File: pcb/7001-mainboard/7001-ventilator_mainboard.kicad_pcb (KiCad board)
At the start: 4 copper layers, 84 parts, among them J1 USB_B_Micro, J10 UART, J2 SWD, J3 Conn_01x02_MountingPin, J4 DNI, J6 5V out, J9 Raspberry_Pi_2_3, Q1 IRLML6244TRPbF, U1 MPRLS0001PG0000SA, U10 ABPMAND001PG2A3, U11 MPVZ5010GW6U, U12 MPVZ5010GW6U, U2 TPD2E2U06, U3 LPC11U37FBD48-401_, U4 MCP1825S, U7 AD5410AREZ, U8 MPRLS0001PG0000SA, U9 ABPMAND001PG2A3, Y1 MCSJK-7U-12.00-10-10-80-B-10

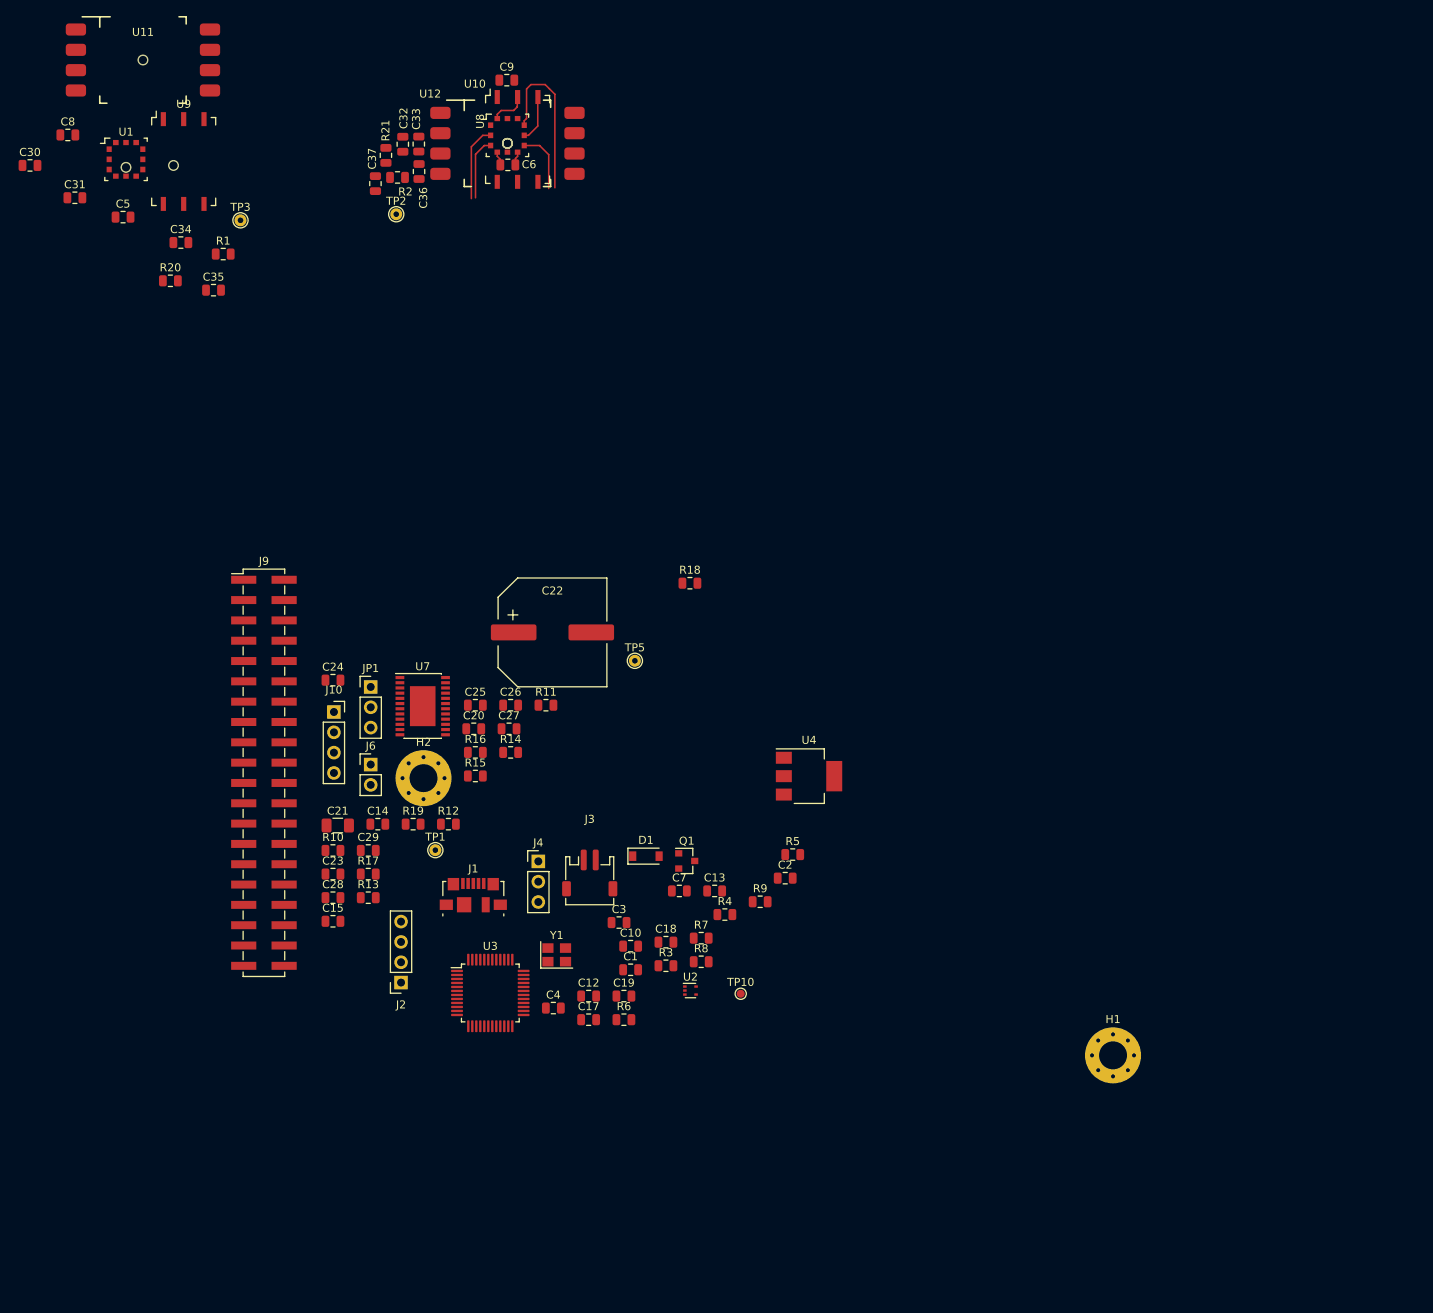
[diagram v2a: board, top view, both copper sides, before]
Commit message: Schematics/PCB: add screw terminal footprints
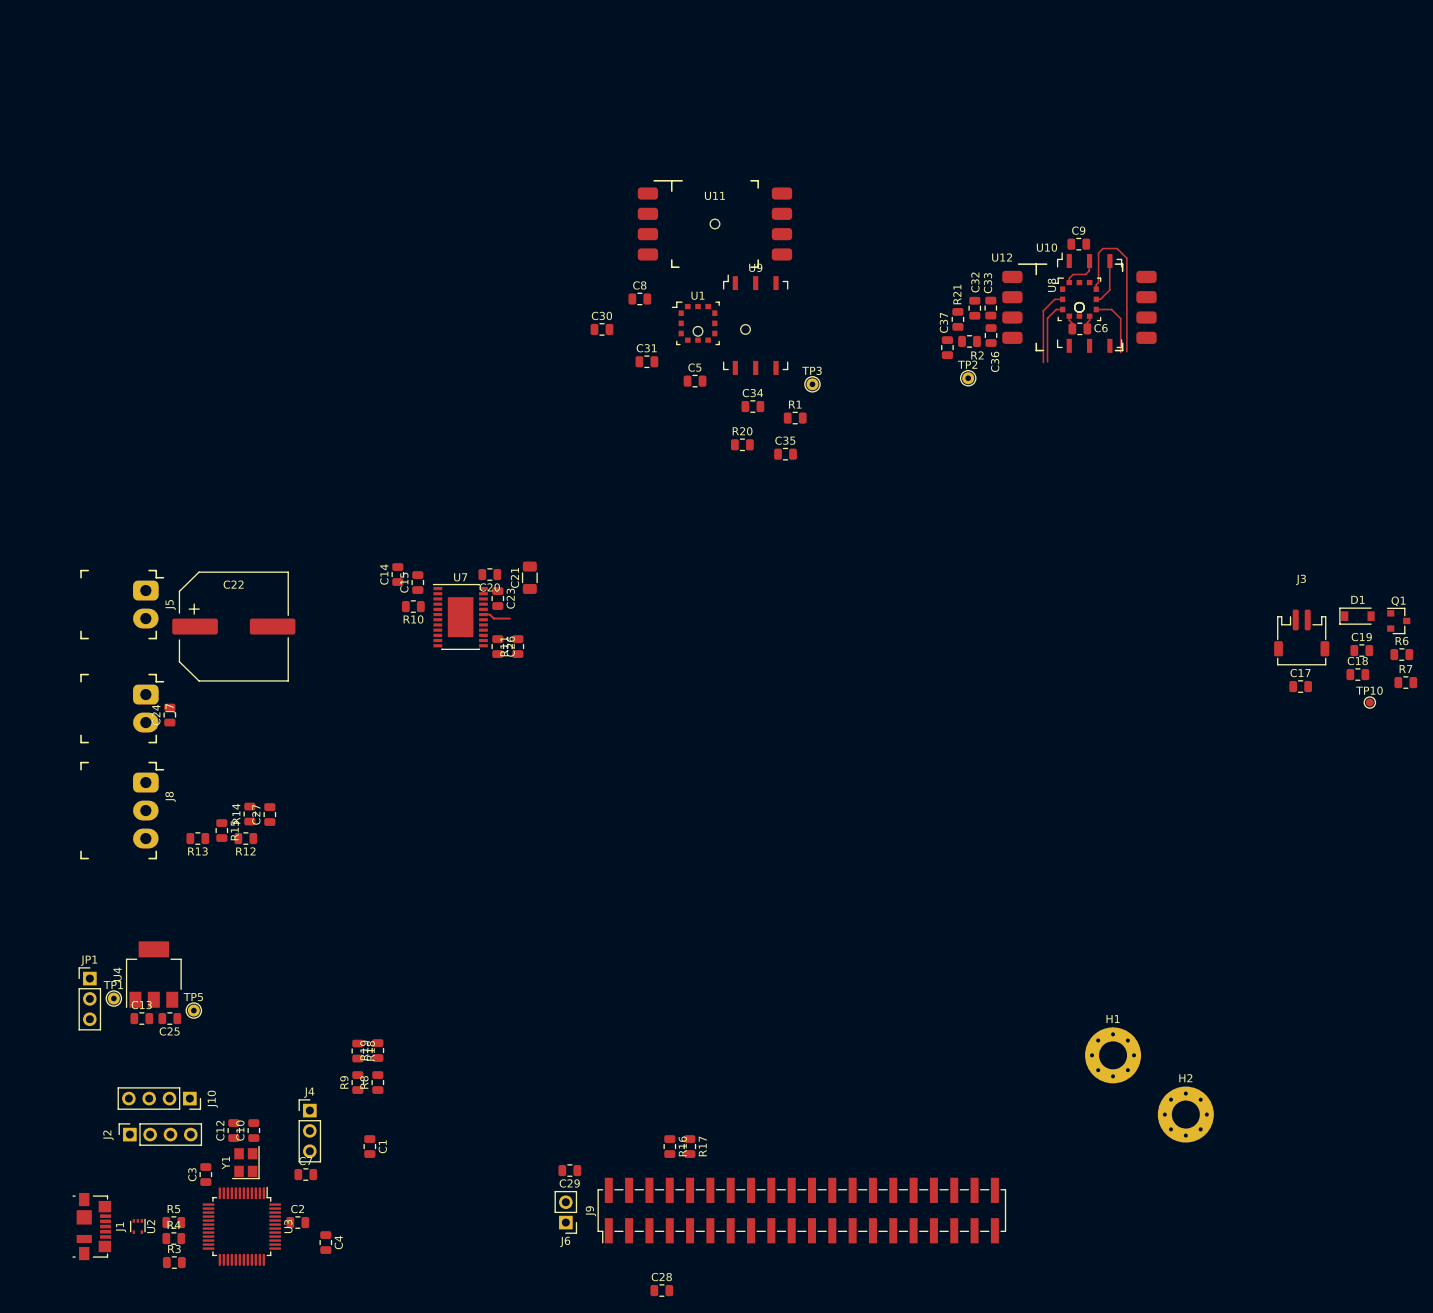
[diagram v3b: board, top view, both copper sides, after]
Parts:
- added J5: 24VIN, Jitter_Footprints:TerminalBlock_Wurth_WR-TBL_691322110002_1x02_P3.50mm_Horizontal, F.Cu at (30.0, 22.0)
- added J7: PREG_PWR, Jitter_Footprints:TerminalBlock_Wurth_WR-TBL_691322110002_1x02_P3.50mm_Horizontal, F.Cu at (30.0, 35.0)
- added J8: PREG_SIGNALS, Jitter_Footprints:TerminalBlock_Wurth_WR-TBL_691322110003_1x03_P3.50mm_Horizontal, F.Cu at (30.0, 46.0)
- moved R6 107.4 mm to (187.0, 30.0)
- moved H2 104.2 mm to (160.0, 87.5)
- moved C19 101.9 mm to (182.0, 29.5)
- moved C17 98.3 mm to (174.3, 34.0)
- moved J3 93.9 mm to (174.5, 28.3)
- moved Q1 93.9 mm to (186.6, 25.8)
- moved D1 93.9 mm to (181.5, 25.2)
- moved R7 93.7 mm to (187.5, 33.5)
- moved C18 92.7 mm to (181.5, 32.5)
- moved R5 90.0 mm to (33.5, 101.0)
- moved J9 86.7 mm to (112.0, 99.5), turned to 90 degrees
- moved TP10 86.7 mm to (183.0, 36.0)
- moved U4 85.6 mm to (31.0, 70.0), turned to 90 degrees
- moved R4 79.9 mm to (33.5, 103.0)
- moved U2 75.1 mm to (29.0, 101.5), turned to 270 degrees
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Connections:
- R13 pad 2: (no net) -> /I_PREG_FEEDBACK
- U7 pad 19: (no net) -> /I_PREG_SETPOINT
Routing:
- net /I_PREG_SETPOINT: track 0.00 -> 3.51 mm

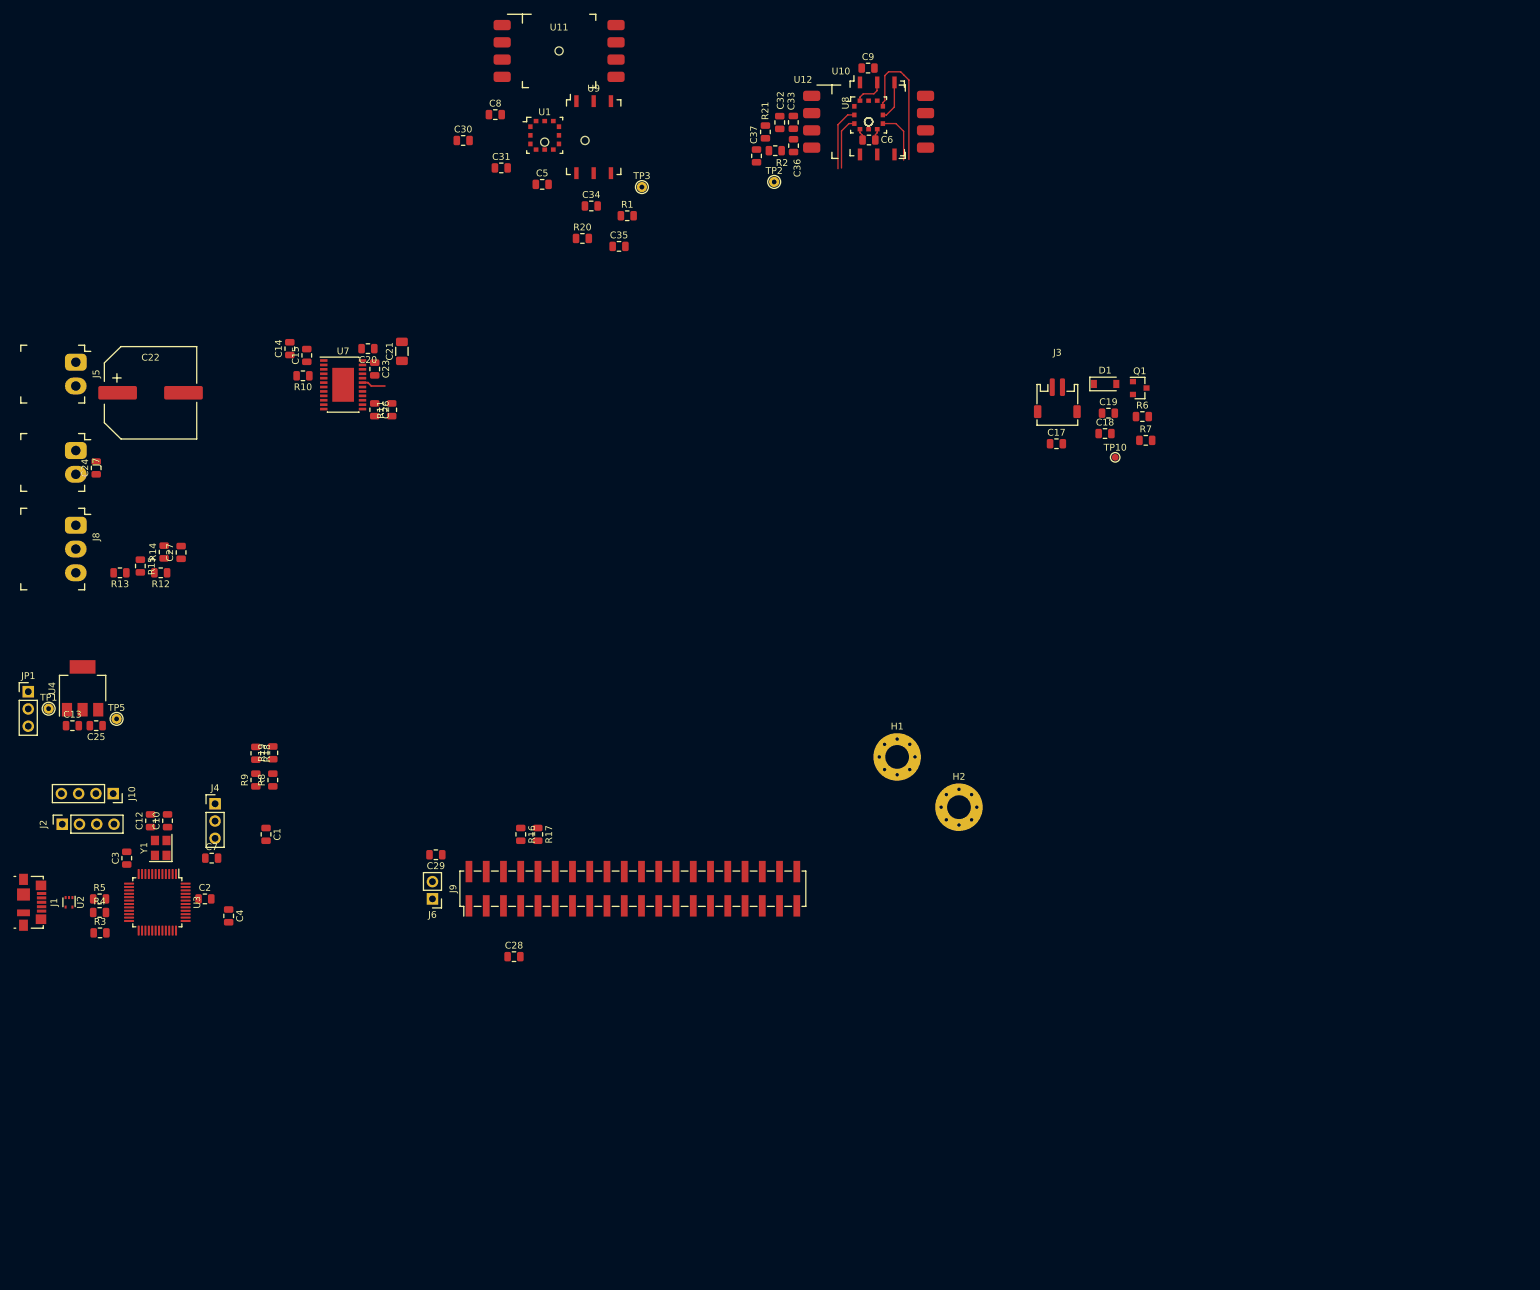
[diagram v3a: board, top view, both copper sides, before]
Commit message: Schematics/PCB: mounting holes, group components in layout
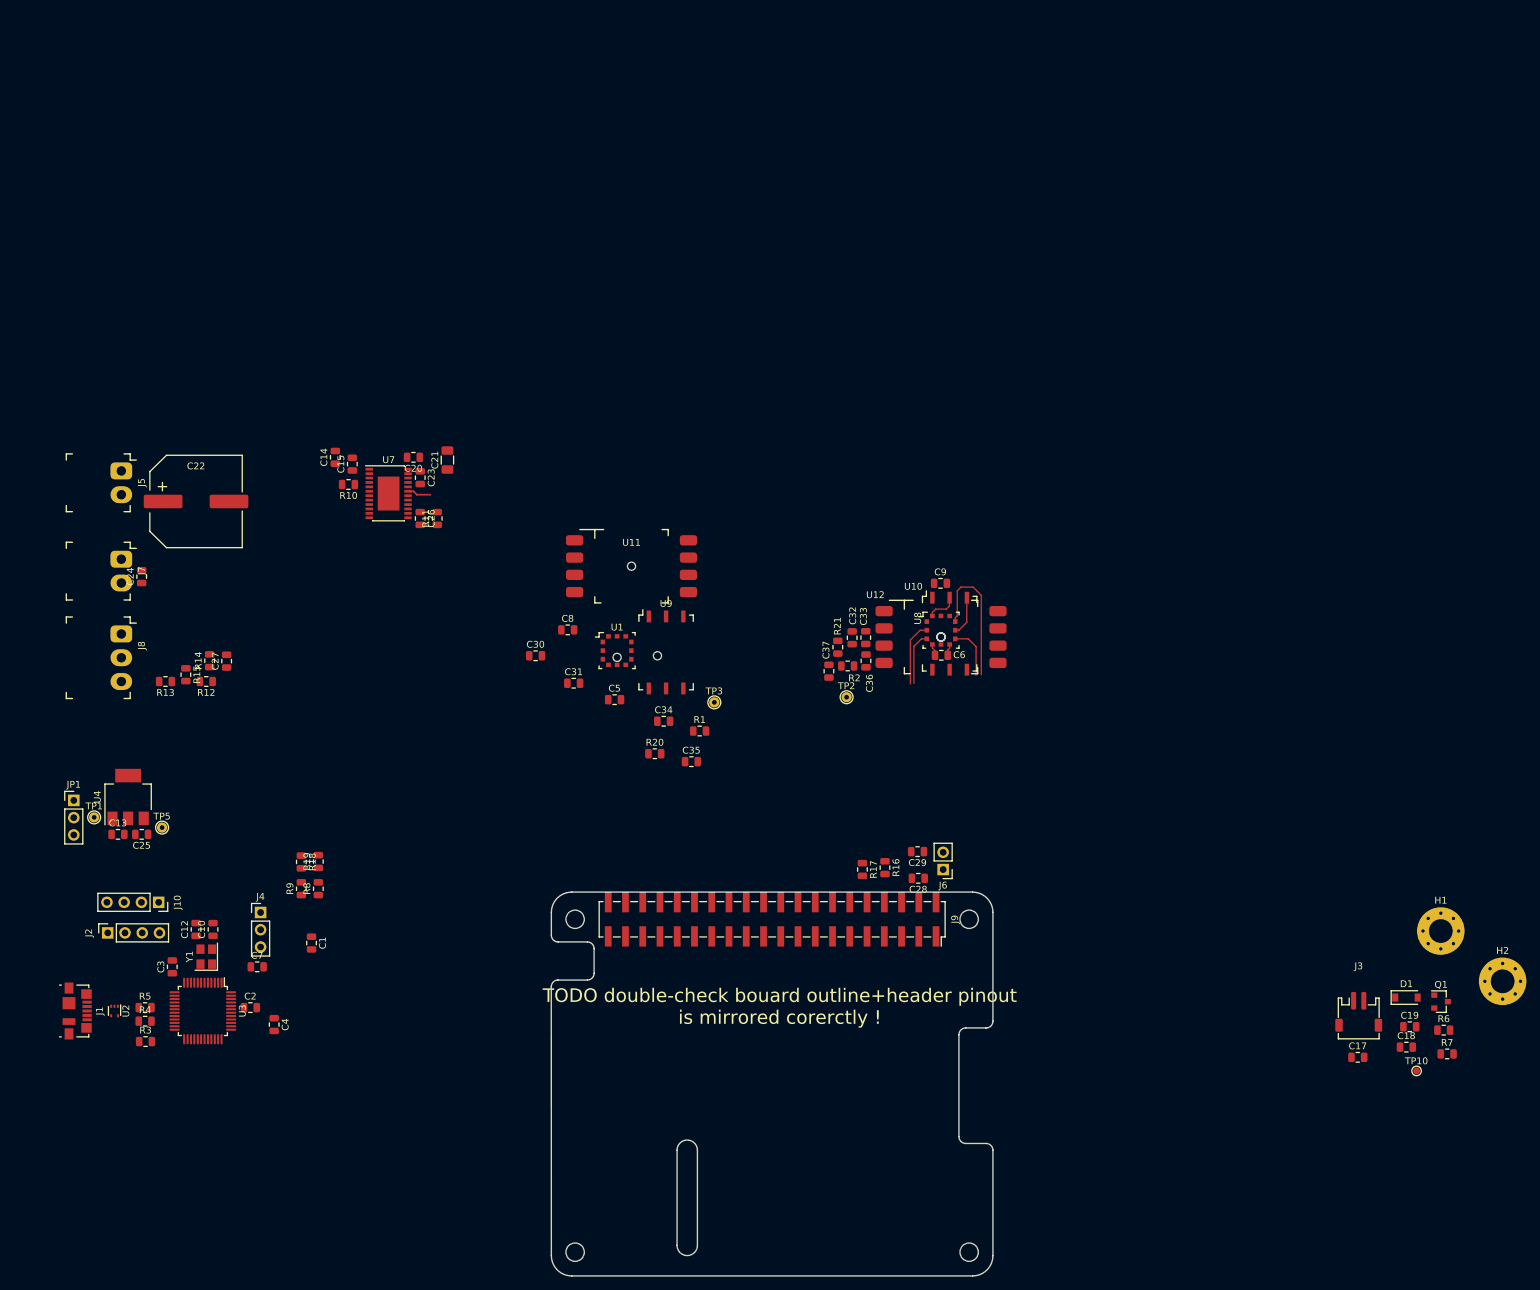
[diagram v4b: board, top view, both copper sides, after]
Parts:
- added H3: DNI, MountingHole:MountingHole_2.7mm_M2.5, B.Cu at (103.5, 153.0)
- added H4: DNI, MountingHole:MountingHole_2.7mm_M2.5, B.Cu at (161.5, 153.0)
- added H5: DNI, MountingHole:MountingHole_2.7mm_M2.5, B.Cu at (161.5, 104.0)
- added H6: DNI, MountingHole:MountingHole_2.7mm_M2.5, B.Cu at (103.5, 104.0)
- J9: footprint Connector_PinHeader_2.54mm:PinHeader_2x20_P2.54mm_Vertical_SMD -> Connector_PinSocket_2.54mm:PinSocket_2x20_P2.54mm_Vertical_SMD
- moved C17 100.6 mm to (218.7, 124.3)
- moved C18 100.6 mm to (225.9, 122.8)
- moved C19 100.6 mm to (226.4, 119.8)
- moved D1 100.6 mm to (225.9, 115.5)
- moved J3 100.6 mm to (218.8, 118.6)
- moved Q1 100.6 mm to (231.0, 116.1)
- moved R6 100.6 mm to (231.4, 120.3)
- moved R7 100.6 mm to (231.9, 123.8)
- moved TP10 100.6 mm to (227.4, 126.3)
- moved H1 84.0 mm to (230.9, 105.7)
- moved H2 84.0 mm to (240.0, 113.1)
- moved C37 76.6 mm to (140.9, 67.5)
- moved U12 76.6 mm to (157.4, 62.5)
- moved U8 76.6 mm to (157.4, 61.5)
- moved C30 76.6 mm to (97.7, 65.2)
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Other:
- board outline added: 65 x 56.5 mm
- board text added: "TODO double-check bouard outline+header pinout is mirrored corerctly !"

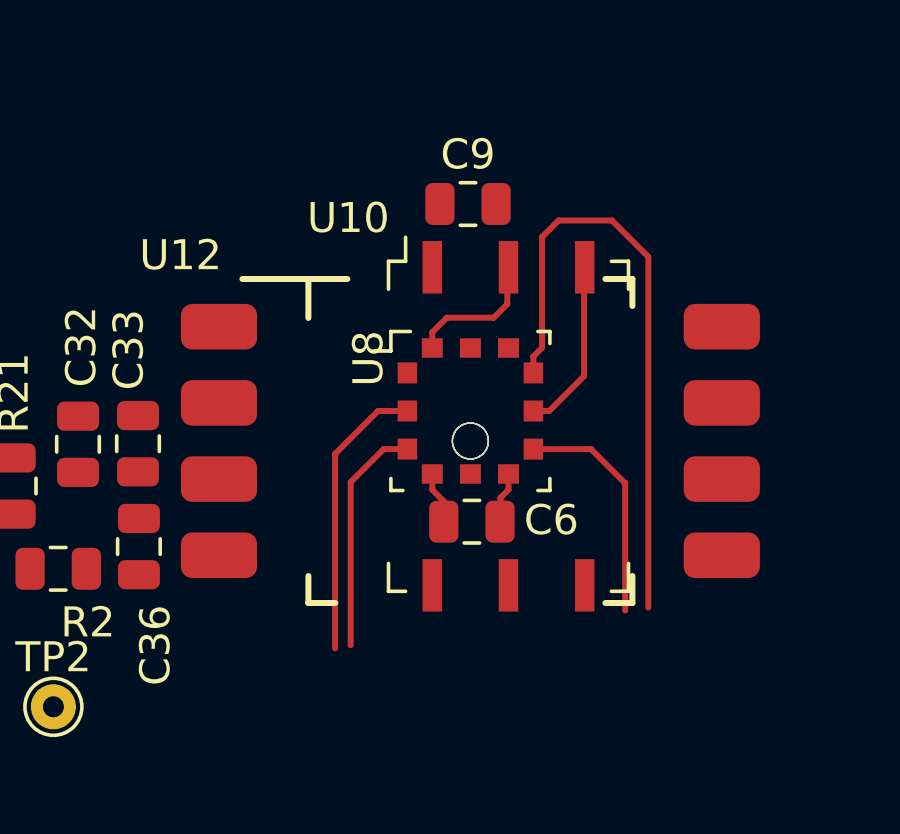
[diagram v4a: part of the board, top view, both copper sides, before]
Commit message: Schematics: add 24v,12v power supplies, etc
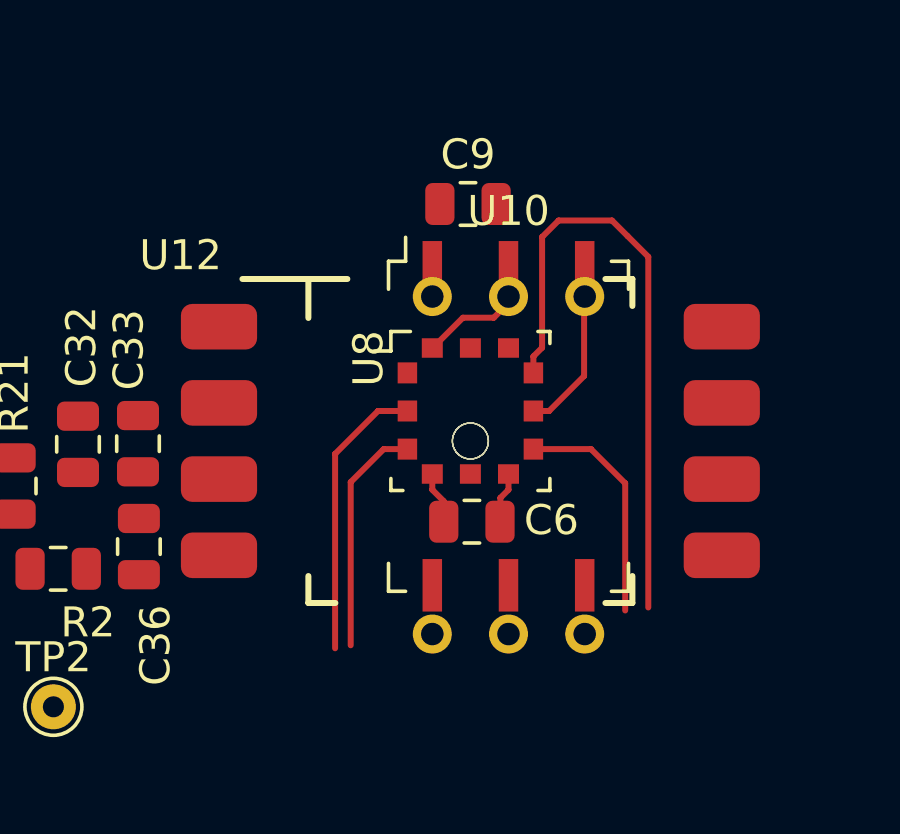
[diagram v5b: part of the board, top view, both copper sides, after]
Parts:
- U10: footprint Jitter_Footprints:ABPMXXX000XX0XX -> Jitter_Footprints:ABPM+DXXX000XX0XX
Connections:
- U10 pad 4: (no net) -> Net-(U10-Pad4)
